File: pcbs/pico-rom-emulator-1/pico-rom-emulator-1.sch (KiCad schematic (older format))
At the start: 6 parts

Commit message: PCB updates
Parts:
- added C1, C2, C3, C4, C5: C_Small, Capacitor_SMD:C_0805_2012Metric_Pad1.15x1.40mm_HandSolder, symbol Device:C_Small
- added J1, J2: Conn_01x03_Female, Connector_PinHeader_2.54mm:PinHeader_1x03_P2.54mm_Vertical, symbol Connector:Conn_01x03_Female
- added R1, R2, R3, R4, R5, R6: R_Small, Resistor_SMD:R_0805_2012Metric_Pad1.15x1.40mm_HandSolder, symbol Device:R_Small
- U1, U2, U4, U5: renamed from U?; footprint (none) -> Package_SO:SOIC-20W_7.5x12.8mm_P1.27mm
- U6: renamed from U?; footprint RPi_Pico:RPi_Pico_SMD_TH -> rp2040:RPi_Pico_SMD_TH
- gave numbers to parts that had none: 1
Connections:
- net +3V3: now also C1.1, C2.1, C3.1, C4.1, C5.1, R1.1, R2.1, R5.1
- net A15: now also U3.1 (A15)
- net EMA14: no longer U3.27 (A14)
- net EMA15: no longer U3.1 (A15)
- net EMOE: now also J1.1 (Pin_1)
- net GND: now also C1.2, C2.2, C3.2, C4.2, C5.2, J2.2 (Pin_2), R3.2, R4.2, R6.2
- net at U2.1 (A->B): now also R1.2
- net at U2.19 (CE): now also R4.1
- net at U1.1 (A->B): now also R2.2
- net at U1.19 (CE): now also R3.1
- net DATA_DIR: now reaches U4.1 (A->B)
- net at U4.19 (CE): now also J1.2 (Pin_2)
- net at U5.1 (A->B): now also R5.2
- net at U5.19 (CE): now also R6.1
- net at U6.41 (SWCLK): now also J2.3 (Pin_3)
- net at U6.43 (SWDIO): now also J2.1 (Pin_1)
- new net A14_OE: J1.3 (Pin_3), U3.27 (A14)

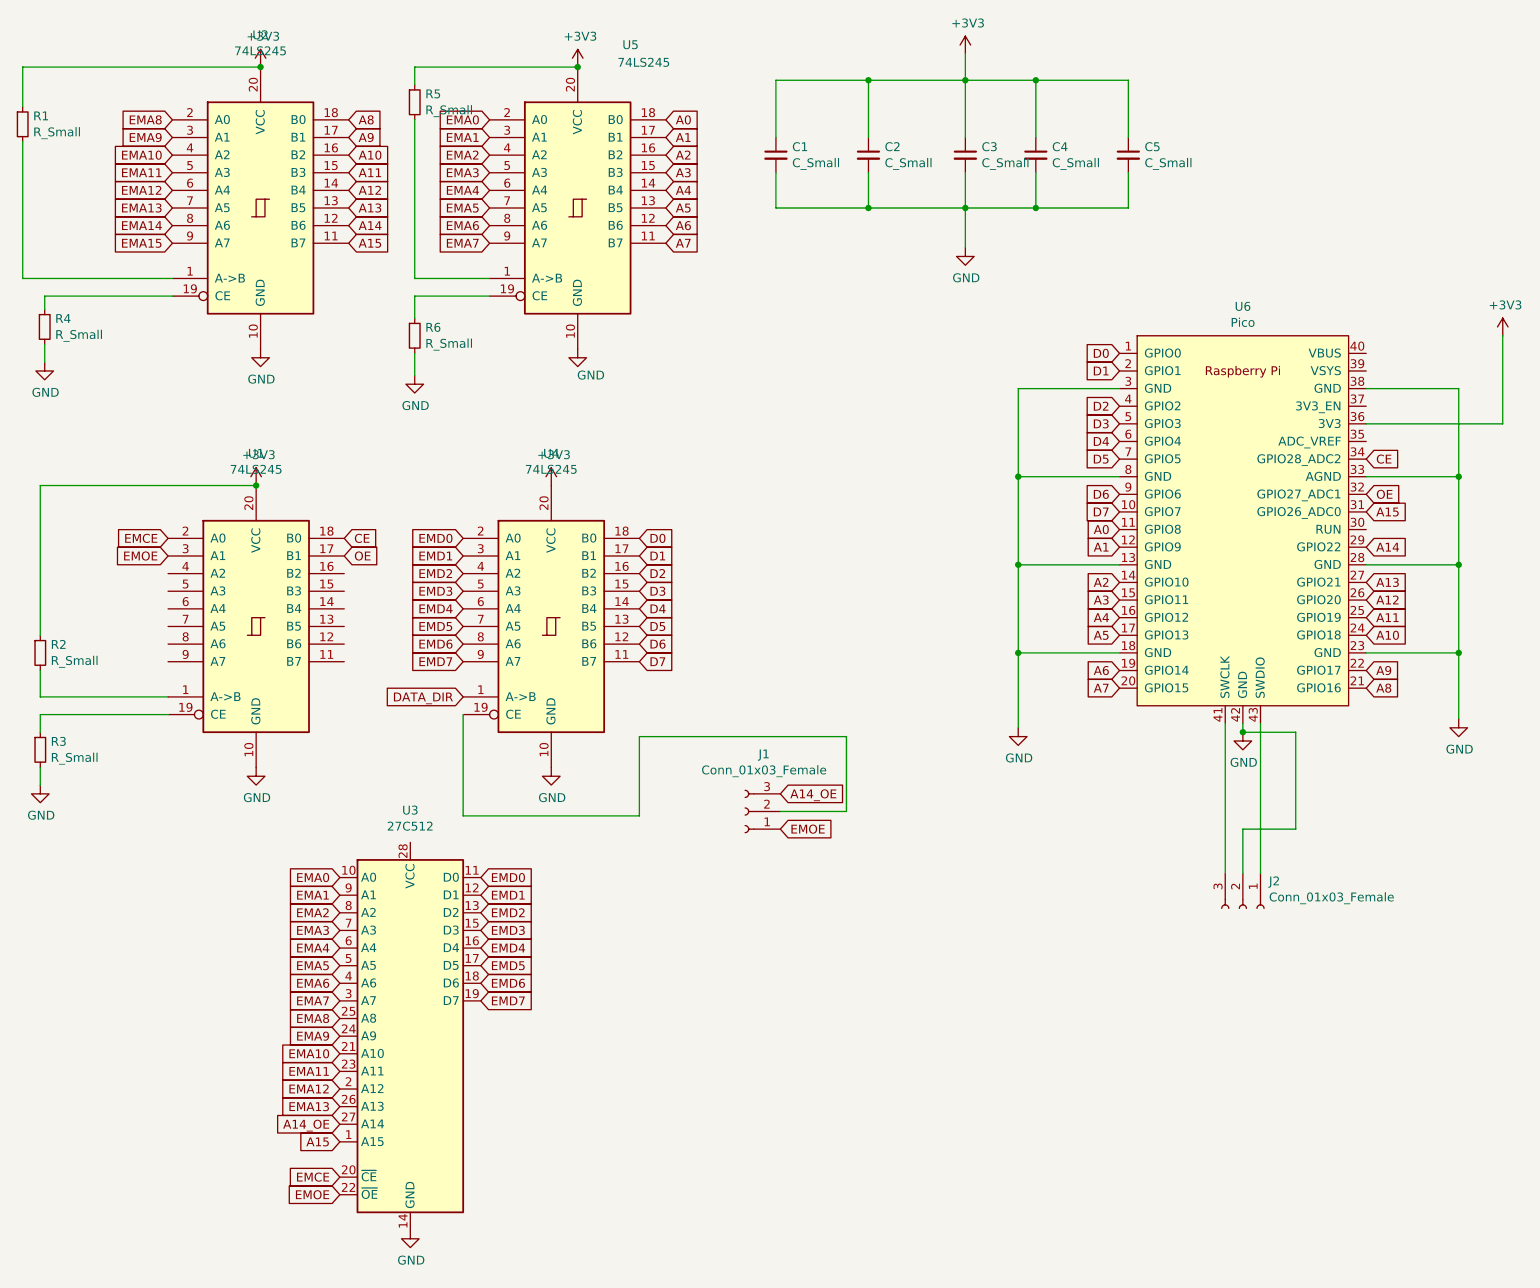
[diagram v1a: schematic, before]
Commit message: Added C code for emulator
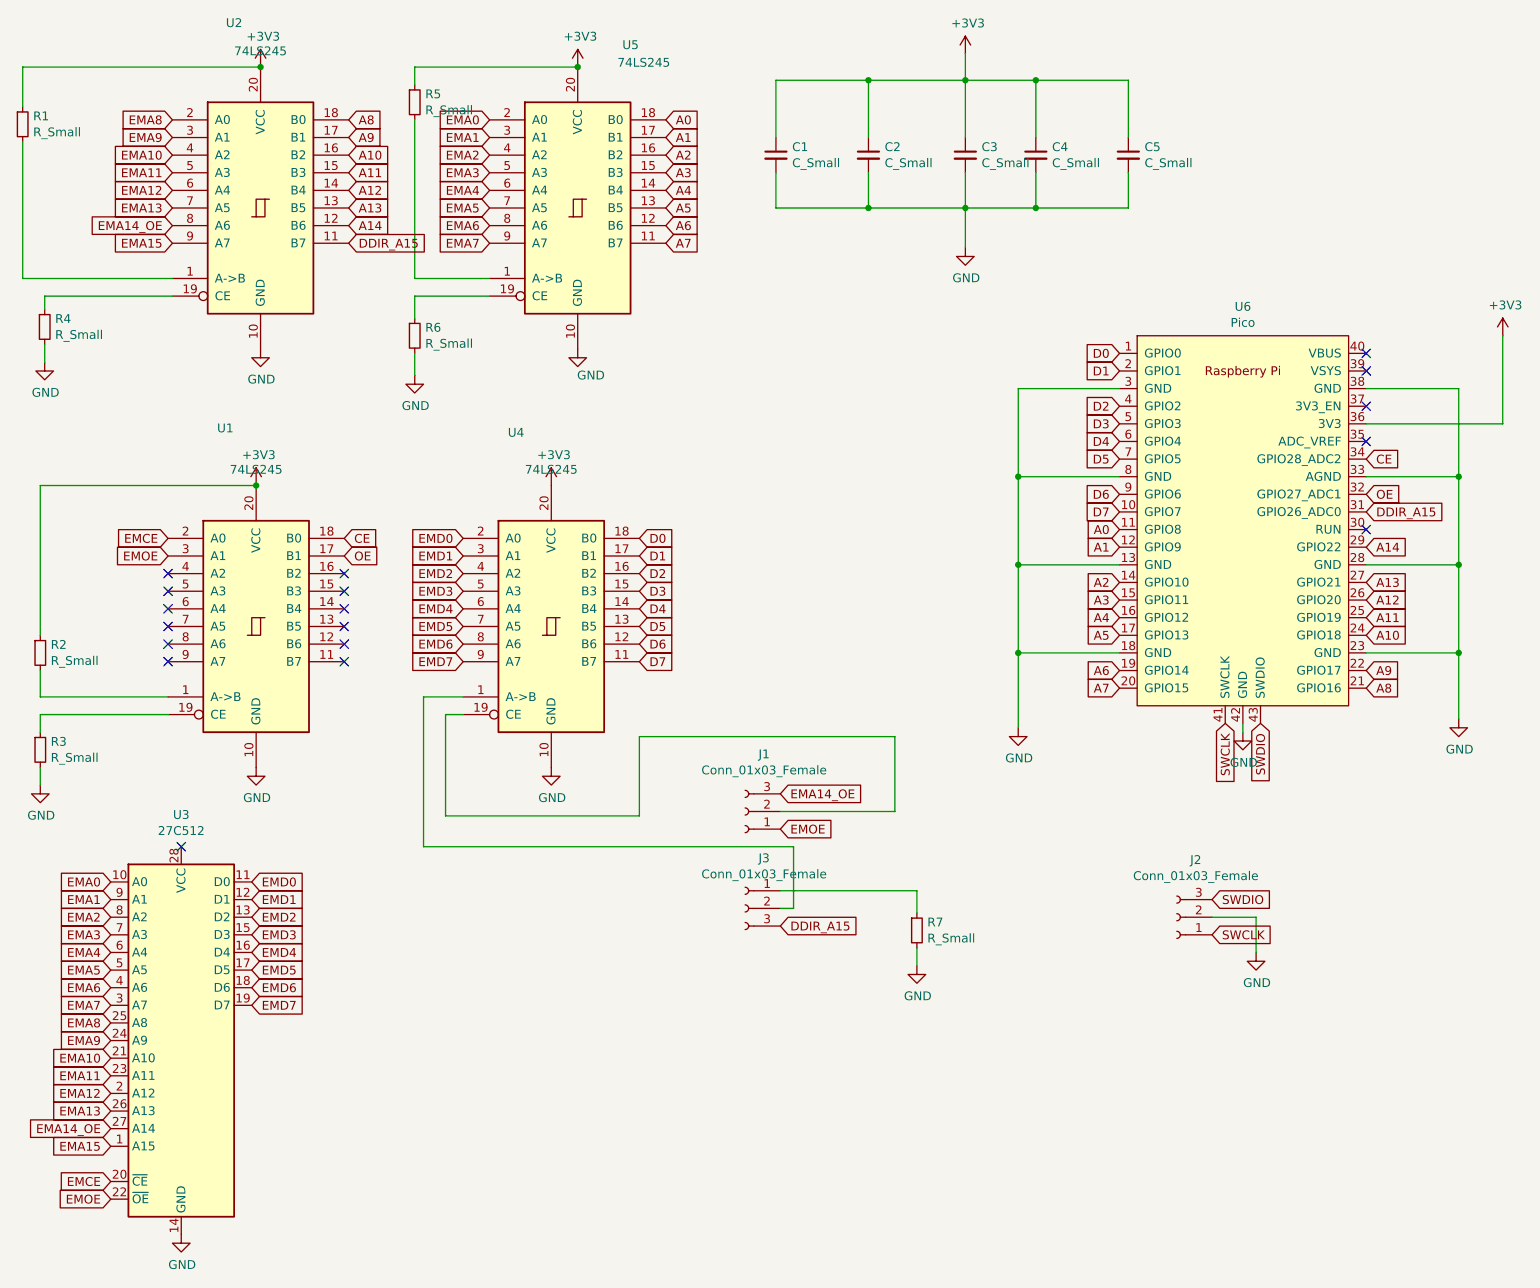
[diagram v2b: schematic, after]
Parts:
- added J3: Conn_01x03_Female, Connector_PinHeader_2.54mm:PinHeader_1x03_P2.54mm_Vertical, symbol Connector:Conn_01x03_Female
- added R7: R_Small, Resistor_SMD:R_0805_2012Metric_Pad1.15x1.40mm_HandSolder, symbol Device:R_Small
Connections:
- net EMA14 is gone; now on net EMA14_OE: U2.8 (A6)
- net EMA15: now also U3.1 (A15)
- net GND: now also R7.2
- net SWCLK: now reaches U6.41 (SWCLK)
- net SWCLK: now also J2.1 (Pin_1); no longer J2.3 (Pin_3)
- net SWDIO: now reaches U6.43 (SWDIO)
- net SWDIO: now also J2.3 (Pin_3); no longer J2.1 (Pin_1)
- net A14_OE renamed EMA14_OE
- net A15 renamed DDIR_A15
- net DDIR_A15: now also J3.3 (Pin_3); no longer U3.1 (A15)
- net DATA_DIR: no longer names the net of U4.1 (A->B)
- net DATA_DIR: now also J3.2 (Pin_2)
- new net: J3.1 (Pin_1), R7.1
- no-connect marks 0 -> 18
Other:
- moved on the sheet: J2, U3
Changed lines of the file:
@@
 U 1 1 61236888
 P 2350 1675
-F 0 "U2" H 2350 2656 50  0000 C CNN
+F 0 "U2" H 2200 2725 50  0000 C CNN
 F 1 "74LS245" H 2350 2565 50  0000 C CNN
 F 2 "Package_SO:SOIC-20W_7.5x12.8mm_P1.27mm" H 2350 1675 50  0001 C CNN
@@
 U 1 1 612370CD
 P 2325 4050
-F 0 "U1" H 2325 5031 50  0000 C CNN
+F 0 "U1" H 2150 5175 50  0000 C CNN
 F 1 "74LS245" H 2325 4940 50  0000 C CNN
 F 2 "Package_SO:SOIC-20W_7.5x12.8mm_P1.27mm" H 2325 4050 50  0001 C CNN
@@
 U 1 1 61237B81
 P 4000 4050
-F 0 "U4" H 4000 5031 50  0000 C CNN
+F 0 "U4" H 3800 5150 50  0000 C CNN
 F 1 "74LS245" H 4000 4940 50  0000 C CNN
 F 2 "Package_SO:SOIC-20W_7.5x12.8mm_P1.27mm" H 4000 4050 50  0001 C CNN
@@
 L Memory_EPROM:27C512 U3
 U 1 1 611F9EB4
-P 3200 6375
-F 0 "U3" H 3200 7656 50  0000 C CNN
-F 1 "27C512" H 3200 7565 50  0000 C CNN
-F 2 "Package_DIP:DIP-28_W15.24mm" H 3200 6375 50  0001 C CNN
-F 3 "http://ww1.microchip.com/downloads/en/DeviceDoc/doc0015.pdf" H 3200 6375 50  0001 C CNN
-	1    3200 6375
+P 1900 6400
+F 0 "U3" H 1900 7681 50  0000 C CNN
+F 1 "27C512" H 1900 7590 50  0000 C CNN
+F 2 "Package_DIP:DIP-28_W15.24mm" H 1900 6400 50  0001 C CNN
+F 3 "http://ww1.microchip.com/downloads/en/DeviceDoc/doc0015.pdf" H 1900 6400 50  0001 C CNN
+	1    1900 6400
 	1    0    0    -1
 $EndComp
@@
 L power:GND #PWR0101
 U 1 1 611FB6EE
-P 3200 7475
-F 0 "#PWR0101" H 3200 7225 50  0001 C CNN
-F 1 "GND" H 3205 7302 50  0000 C CNN
-F 2 "" H 3200 7475 50  0001 C CNN
-F 3 "" H 3200 7475 50  0001 C CNN
-	1    3200 7475
+P 1900 7500
+F 0 "#PWR0101" H 1900 7250 50  0001 C CNN
+F 1 "GND" H 1905 7327 50  0000 C CNN
+F 2 "" H 1900 7500 50  0001 C CNN
+F 3 "" H 1900 7500 50  0001 C CNN
+	1    1900 7500
 	1    0    0    -1
 $EndComp
@@
 Text GLabel 8625 3800 2    50   Input ~ 0
 A13
-Text GLabel 2800 6975 0    50   Input ~ 0
-A15
 Text GLabel 8625 3300 2    50   Input ~ 0
 OE
@@
 A14
 Text GLabel 2850 1875 2    50   Input ~ 0
-A15
+DDIR_A15
 Text GLabel 3650 1175 0    50   Input ~ 0
 EMA0
@@
 EMA13
 Text GLabel 1850 1775 0    50   Input ~ 0
-EMA14
+EMA14_OE
 Text GLabel 1850 1875 0    50   Input ~ 0
 EMA15
@@
 Text GLabel 1825 3650 0    50   Input ~ 0
 EMOE
-Text GLabel 3600 5475 2    50   Input ~ 0
+Text GLabel 2300 5500 2    50   Input ~ 0
 EMD0
-Text GLabel 3600 5575 2    50   Input ~ 0
+Text GLabel 2300 5600 2    50   Input ~ 0
 EMD1
-Text GLabel 3600 5675 2    50   Input ~ 0
+Text GLabel 2300 5700 2    50   Input ~ 0
 EMD2
-Text GLabel 3600 5775 2    50   Input ~ 0
+Text GLabel 2300 5800 2    50   Input ~ 0
 EMD3
-Text GLabel 3600 5875 2    50   Input ~ 0
+Text GLabel 2300 5900 2    50   Input ~ 0
 EMD4
-Text GLabel 3600 5975 2    50   Input ~ 0
+Text GLabel 2300 6000 2    50   Input ~ 0
 EMD5
-Text GLabel 3600 6075 2    50   Input ~ 0
+Text GLabel 2300 6100 2    50   Input ~ 0
 EMD6
-Text GLabel 3600 6175 2    50   Input ~ 0
+Text GLabel 2300 6200 2    50   Input ~ 0
 EMD7
-Text GLabel 2800 5475 0    50   Input ~ 0
+Text GLabel 1500 5500 0    50   Input ~ 0
 EMA0
-Text GLabel 2800 5575 0    50   Input ~ 0
+Text GLabel 1500 5600 0    50   Input ~ 0
 EMA1
-Text GLabel 2800 5675 0    50   Input ~ 0
+Text GLabel 1500 5700 0    50   Input ~ 0
 EMA2
-Text GLabel 2800 5775 0    50   Input ~ 0
+Text GLabel 1500 5800 0    50   Input ~ 0
 EMA3
-Text GLabel 2800 5875 0    50   Input ~ 0
+Text GLabel 1500 5900 0    50   Input ~ 0
 EMA4
-Text GLabel 2800 5975 0    50   Input ~ 0
+Text GLabel 1500 6000 0    50   Input ~ 0
 EMA5
-Text GLabel 2800 6075 0    50   Input ~ 0
+Text GLabel 1500 6100 0    50   Input ~ 0
 EMA6
-Text GLabel 2800 6175 0    50   Input ~ 0
+Text GLabel 1500 6200 0    50   Input ~ 0
 EMA7
-Text GLabel 2800 6275 0    50   Input ~ 0
+Text GLabel 1500 6300 0    50   Input ~ 0
 EMA8
-Text GLabel 2800 6375 0    50   Input ~ 0
+Text GLabel 1500 6400 0    50   Input ~ 0
 EMA9
-Text GLabel 2800 6475 0    50   Input ~ 0
+Text GLabel 1500 6500 0    50   Input ~ 0
 EMA10
-Text GLabel 2800 6575 0    50   Input ~ 0
+Text GLabel 1500 6600 0    50   Input ~ 0
 EMA11
-Text GLabel 2800 6675 0    50   Input ~ 0
+Text GLabel 1500 6700 0    50   Input ~ 0
 EMA12
-Text GLabel 2800 6775 0    50   Input ~ 0
+Text GLabel 1500 6800 0    50   Input ~ 0
 EMA13
-Text GLabel 2800 7175 0    50   Input ~ 0
+Text GLabel 1500 7200 0    50   Input ~ 0
 EMCE
-Text GLabel 2800 7275 0    50   Input ~ 0
+Text GLabel 1500 7300 0    50   Input ~ 0
 EMOE
-Text GLabel 3500 4450 0    50   Input ~ 0
-DATA_DIR
 Text GLabel 5300 5200 2    50   Input ~ 0
 EMOE
@@
 $EndComp
 Wire Wire Line
-	5300 5100 5675 5100
-Wire Wire Line
-	5675 5100 5675 4675
-Wire Wire Line
-	5675 4675 4500 4675
-Wire Wire Line
 	4500 4675 4500 5125
-Wire Wire Line
-	4500 5125 3500 5125
-Wire Wire Line
-	3500 5125 3500 4550
 $Comp
 L Device:R_Small R2
@@
 Wire Wire Line
 	1100 4550 1825 4550
-Text GLabel 8625 3400 2    50   Input ~ 0
-A15
 Text GLabel 5300 5000 2    50   Input ~ 0
-A14_OE
+EMA14_OE
 Text GLabel 8625 3600 2    50   Input ~ 0
 A14
-Text GLabel 2800 6875 0    50   Input ~ 0
-A14_OE
+Text GLabel 1500 6900 0    50   Input ~ 0
+EMA14_OE
 $Comp
 L Device:C_Small C1
@@
 L Connector:Conn_01x03_Female J2
 U 1 1 6125BDB8
-P 7925 5650
-F 0 "J2" V 7771 5798 50  0000 L CNN
-F 1 "Conn_01x03_Female" V 7862 5798 50  0000 L CNN
-F 2 "Connector_PinHeader_2.54mm:PinHeader_1x03_P2.54mm_Vertical" H 7925 5650 50  0001 C CNN
-F 3 "~" H 7925 5650 50  0001 C CNN
-	1    7925 5650
-	0    1    1    0
-$EndComp
-Wire Wire Line
-	7825 4600 7825 5450
-Wire Wire Line
-	8025 4600 8025 5450
-Wire Wire Line
-	7925 4650 8225 4650
-Wire Wire Line
-	8225 4650 8225 5200
-Wire Wire Line
-	8225 5200 7925 5200
-Wire Wire Line
-	7925 5200 7925 5450
-Connection ~ 7925 4650
+P 7550 5700
+F 0 "J2" H 7442 5375 50  0000 C CNN
+F 1 "Conn_01x03_Female" H 7442 5466 50  0000 C CNN
+F 2 "Connector_PinHeader_2.54mm:PinHeader_1x03_P2.54mm_Vertical" H 7550 5700 50  0001 C CNN
+F 3 "~" H 7550 5700 50  0001 C CNN
+	1    7550 5700
+	-1   0    0    1
+$EndComp
+Text GLabel 8625 3400 2    50   Input ~ 0
+DDIR_A15
+$Comp
+L Connector:Conn_01x03_Female J3
+U 1 1 6126F915
+P 5100 5650
+F 0 "J3" H 4992 5935 50  0000 C CNN
+F 1 "Conn_01x03_Female" H 4992 5844 50  0000 C CNN
+F 2 "Connector_PinHeader_2.54mm:PinHeader_1x03_P2.54mm_Vertical" H 5100 5650 50  0001 C CNN
+F 3 "~" H 5100 5650 50  0001 C CNN
+	1    5100 5650
+	-1   0    0    -1
+$EndComp
+Wire Wire Line
+	5375 5650 5300 5650
+Wire Wire Line
+	4500 5125 3400 5125
+Wire Wire Line
+	3400 5125 3400 4550
+Wire Wire Line
+	3400 4550 3500 4550
+Wire Wire Line
+	5375 5300 3275 5300
+Wire Wire Line
+	3275 5300 3275 4450
+Wire Wire Line
+	3275 4450 3500 4450
+Wire Wire Line
+	5375 5300 5375 5650
+Wire Wire Line
+	5950 5100 5950 4675
+Wire Wire Line
+	5300 5100 5950 5100
+Wire Wire Line
+	4500 4675 5950 4675
+Text GLabel 5300 5750 2    50   Input ~ 0
+DDIR_A15
+$Comp
+L Device:R_Small R7
+U 1 1 61282E0C
+P 6075 5775
+F 0 "R7" H 6134 5821 50  0000 L CNN
+F 1 "R_Small" H 6134 5730 50  0000 L CNN
+F 2 "Resistor_SMD:R_0805_2012Metric_Pad1.15x1.40mm_HandSolder" H 6075 5775 50  0001 C CNN
+F 3 "~" H 6075 5775 50  0001 C CNN
+	1    6075 5775
+	1    0    0    -1
+$EndComp
+$Comp
+L power:GND #PWR0117
+U 1 1 61282E12
+P 6075 5975
+F 0 "#PWR0117" H 6075 5725 50  0001 C CNN
+F 1 "GND" H 6080 5802 50  0000 C CNN
+F 2 "" H 6075 5975 50  0001 C CNN
+F 3 "" H 6075 5975 50  0001 C CNN
+	1    6075 5975
+	1    0    0    -1
+$EndComp
+Wire Wire Line
+	6075 5975 6075 5875
+Wire Wire Line
+	6075 5550 6075 5675
+Wire Wire Line
+	5300 5550 6075 5550
+Text GLabel 1500 7000 0    50   Input ~ 0
+EMA15
+NoConn ~ 2825 3750
+NoConn ~ 2825 3850
+NoConn ~ 2825 3950
+NoConn ~ 2825 4050
+NoConn ~ 2825 4150
+NoConn ~ 2825 4250
+NoConn ~ 1825 3750
+NoConn ~ 1825 3850
+NoConn ~ 1825 3950
+NoConn ~ 1825 4050
+NoConn ~ 1825 4150
+NoConn ~ 1825 4250
+NoConn ~ 8625 2500
+NoConn ~ 8625 2600
+NoConn ~ 8625 2800
+NoConn ~ 8625 3000
+NoConn ~ 8625 3500
+NoConn ~ 1900 5300
+$Comp
+L power:GND #PWR0118
+U 1 1 612C4853
+P 8000 5900
+F 0 "#PWR0118" H 8000 5650 50  0001 C CNN
+F 1 "GND" H 8005 5727 50  0000 C CNN
+F 2 "" H 8000 5900 50  0001 C CNN
+F 3 "" H 8000 5900 50  0001 C CNN
+	1    8000 5900
+	1    0    0    -1
+$EndComp
+Wire Wire Line
+	7750 5700 8000 5700
+Wire Wire Line
+	8000 5700 8000 5900
+Text GLabel 7825 4600 3    50   Input ~ 0
+SWCLK
+Text GLabel 7750 5800 2    50   Input ~ 0
+SWCLK
+Text GLabel 8025 4600 3    50   Input ~ 0
+SWDIO
+Text GLabel 7750 5600 2    50   Input ~ 0
+SWDIO
 $EndSCHEMATC
